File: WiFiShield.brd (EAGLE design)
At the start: 68.6 x 53.3 mm, 38 parts, among them IC1 74HC4050D, IC2 SPX3819M5-L-3-3, IC3 CC3000MOD, IC4 MCP9701A, J1 Test, J10 U.FL-R-SMT-1(10), J11 Mode, J12 Temp, J5 ARDUINO-SHIELD_R3, J6 101-00660-68-6

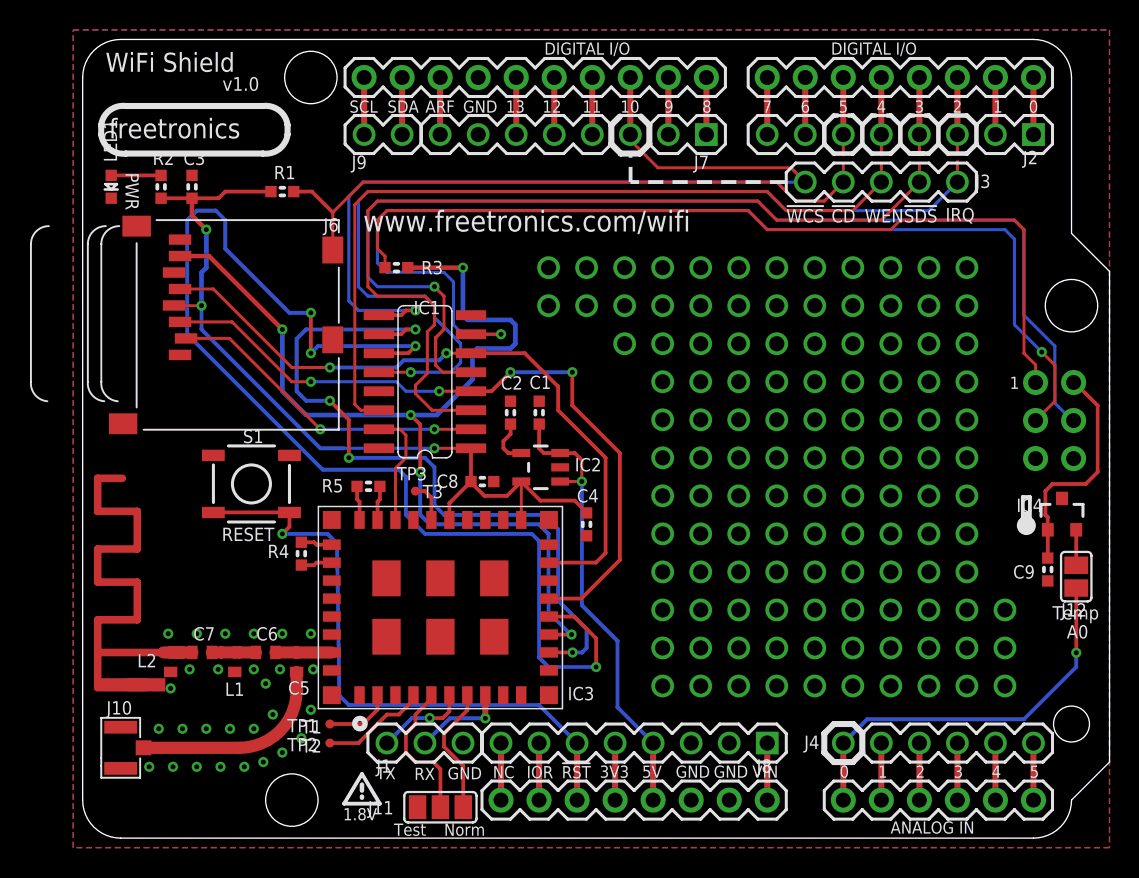
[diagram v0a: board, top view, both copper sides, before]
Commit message: Added tristate buffer on MISO to fix CC3000 SPI bug, some minor tweaks, pull-ups added on nCS lines and CC3000 enable, silkscreen label tweaks.
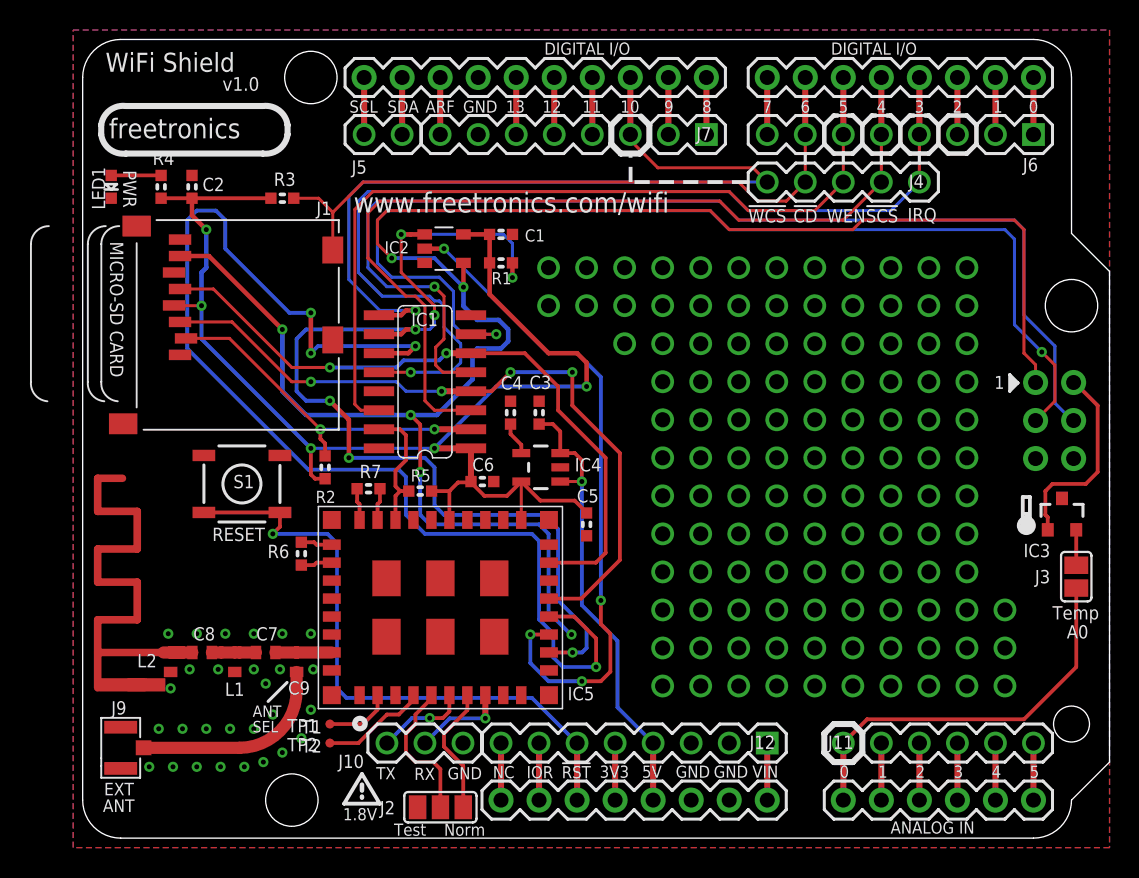
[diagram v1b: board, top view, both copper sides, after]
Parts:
- removed TP3: R3, testpad:TP06R
- added IC5: CC3000MOD, freetronics-luke:CC3000
- added R6, R7: 0R, freetronics-master-v1:0603
- C2: value 10nF -> 100nF
- C4: value 1µF -> 10nF
- C5: value NP -> 1uF; device freetronics-master-v1:C0402 -> freetronics-master-v1:0603
- C6: value 10pF -> 1uF; device freetronics-master-v1:C0402 -> freetronics-master-v1:0603
- C7: value 2.2pF -> 10pF
- C8: value 1µF -> 2.2pF; device freetronics-master-v1:0603 -> freetronics-master-v1:C0402
- C9: value 100nF -> NP; device freetronics-master-v1:0603 -> freetronics-master-v1:C0402
- IC2: value SPX3819M5-L-3-3 -> 74AHC1G125; device SparkFun:SOT23-5 -> 74xx-little-de:SOT23-5
- IC3: value CC3000MOD -> MCP9701A; device freetronics-luke:CC3000 -> freetronics-master-v1:SOT23-3
- IC4: value MCP9701A -> SPX3819M5-L-3-3; device freetronics-master-v1:SOT23-3 -> SparkFun:SOT23-5
- J1: value Test -> 101-00660-68-6; device freetronics-master-v1:1X03 -> RAMPSdisplay:ADAFRUIT_MICROSD
- J10: value U.FL-R-SMT-1(10) -> Test; device freetronics-luke:UFL -> freetronics-master-v1:1X03
- J11: value Mode -> (none); device freetronics-master-v1:SJ_2 -> freetronics-master-v1:1X06
- J12: value Temp -> (none); device freetronics-luke:SJ -> freetronics-master-v1:1X08
- J2: value (none) -> Mode; device freetronics-master-v1:1X08 -> freetronics-master-v1:SJ_2
- J3: value (none) -> Temp; device freetronics-master-v1:1X05 -> freetronics-luke:SJ
- J4: device freetronics-master-v1:1X06 -> freetronics-master-v1:1X05
- J5: value ARDUINO-SHIELD_R3 -> (none); device freetronics-luke:ARDUINO-SHIELD_R3 -> freetronics-master-v1:1X02
- J6: value 101-00660-68-6 -> (none); device RAMPSdisplay:ADAFRUIT_MICROSD -> freetronics-master-v1:1X08
- J8: value (none) -> ARDUINO-SHIELD_R3; device freetronics-master-v1:1X08 -> freetronics-luke:ARDUINO-SHIELD_R3
- J9: value (none) -> U.FL-R-SMT-1(10); device freetronics-master-v1:1X02 -> freetronics-luke:UFL
- R1: value 10kΩ -> 10k
- R2, R3: value 1kΩ -> 10k
- R4: value 0Ω -> 1k
- R5: value 0Ω -> 10k
- moved J2 59.9 mm to (25.8, 2.06), turned to 0 degrees
- moved C9 50.5 mm to (16.2, 11.7), turned to 90 degrees
- moved J6 46.7 mm to (65.4, 47.0), turned to 180 degrees
- moved J9 45.1 mm to (4.45, 6.03)
- moved IC3 42.0 mm to (67.3, 21.6), turned to 0 degrees
- moved J4 37.8 mm to (57.8, 43.8), turned to 180 degrees
- moved J1 35.1 mm to (19.1, 41.3), turned to 270 degrees
- moved IC4 35.0 mm to (32.5, 24.8), turned to 90 degrees
- moved C3 27.7 mm to (32.4, 28.4), turned to 270 degrees
- moved J3 27.5 mm to (68.3, 17.5), turned to 270 degrees
- moved J11 27.2 mm to (52.7, 6.35)
- moved R4 26.2 mm to (7.14, 43.5)
- moved C2 26.1 mm to (9.21, 43.5), turned to 90 degrees
- moved J5 24.8 mm to (23.2, 47.0), turned to 180 degrees
- moved J12 23.4 mm to (47.6, 6.35), turned to 180 degrees
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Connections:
- removed net MISO_3V3: IC3.13, J6.7, R3.1
- removed net MISO_BUFFERED: J5.MISO, R3.2
- removed net N$21: IC1.9, J3.5
- removed net N$3: IC1.15, IC3.26
- removed net N$35: IC1.2, J6.2
- removed net N$41: IC1.10, IC3.12
- removed net RES_3: IC3.24, TP3.TP
- new net !CC3000_CS_3V3: IC1.10, IC2.1, IC5.12, R1.2
- new net !CC3000_CS_5V: IC1.9, J4.5
- new net !SD_CS_3V3: IC1.2, J1.2, R2.2
- new net CC3000_EN_3V3: IC1.15, IC5.26, R5.2
- new net CC3000_MISO: IC2.2, IC5.13
- new net MISO_TRISTATE: IC2.4, J1.7, J8.MISO
- net !CARD_DET: now also J1.CD1, J4.4, R3.1; no longer J3.4, J6.CD1, R1.1
- net !SDCARD_CS_5V: now also J4.2; no longer J3.2
- net +3V3: now also C1.2, C2.1, C5.1, C6.2, IC4.5, IC5.19, IC5.23, J1.4, R1.1, R2.1, R3.2, R4.2, R5.1; no longer C3.1, C4.1, C8.2, IC3.19, IC3.23, J6.4, R1.2, R2.2
- net +5V: now also C3.2, IC4.1, IC4.3, J12.4, J8.+5V; no longer C1.2, IC2.1, IC2.3, J5.+5V, J8.4
- net +5V-2: now also IC3.1, J8.+5V@0; no longer C9.1, IC4.1, J5.+5V@0
- net A0: now also J11.1, J3.2, J8.A0; no longer J12.2, J4.1, J5.A0
- net CC3000_EN_5V: now also J4.3; no longer J3.3
- net CC3000_IRQ_5V: now also J4.1; no longer J3.1
- net GND: now also C2.2, C3.1, C4.1, C5.2, C6.1, IC2.3, IC3.3, IC4.2, IC5.1, IC5.10, IC5.11, IC5.16, IC5.18, IC5.20, IC5.21, IC5.22, IC5.25, IC5.31, IC5.32, IC5.33, IC5.34, IC5.36, IC5.37, IC5.38, IC5.39, IC5.40, IC5.41, IC5.42, IC5.43, IC5.44, IC5.45, IC5.46, IC5.9, J1.6, J1.MT1, J1.MT2, J10.3, J12.2, J12.3, J2.1, J8.GND, J8.GND@0, J8.GND@1, J8.GND@2, J9.GND, J9.GND@1; no longer C2.1, C3.2, C4.2, C8.1, C9.2, IC2.2, IC3.1, IC3.10, IC3.11, IC3.16, IC3.18, IC3.20, IC3.21, IC3.22, IC3.25, IC3.31, IC3.32, IC3.33, IC3.34, IC3.36, IC3.37, IC3.38, IC3.39, IC3.40, IC3.41, IC3.42, IC3.43, IC3.44, IC3.45, IC3.46, IC3.9, IC4.3, J1.3, J10.GND, J10.GND@1, J11.1, J5.GND, J5.GND@0, J5.GND@1, J5.GND@2, J6.6, J6.MT1, J6.MT2, J8.2, J8.3
- net MOSI_3V3: now also IC5.15, J1.3; no longer IC3.15, J6.3
- net MOSI_5V: now also J8.MOSI; no longer J5.MOSI
- net N$1: now also IC5.27, R7.2; no longer IC3.27, R5.2
- net N$103: now also C7.1, C8.2; no longer C6.1, C7.2
- net N$104: now also C8.1; no longer C7.1
- net N$11: now also IC3.2, J3.1; no longer IC4.2, J12.1
- net N$123: now also J6.6, J8.D5; no longer J2.6, J5.D5
- net N$124: now also J6.7, J8.D6; no longer J2.7, J5.D6
- net N$125: now also J6.8, J8.D7; no longer J2.8, J5.D7
- net N$126: now also J5.1, J8.SDA; no longer J5.SDA, J9.1
- net N$127: now also J8.AREF; no longer J5.AREF
- net N$128: now also J8.D13; no longer J5.D13
- net N$129: now also J8.D12; no longer J5.D12
- net N$130: now also J5.2, J8.SCL; no longer J5.SCL, J9.2
- net N$131: now also J8.D8; no longer J5.D8
- net N$132: now also J8.D9; no longer J5.D9
- net N$133: now also J8.D10; no longer J5.D10
- net N$134: now also J8.D11; no longer J5.D11
- net N$15: now also IC5.30, R6.2; no longer IC3.30, R4.2
- net N$16: now also C7.2, C9.2, IC5.35; no longer C5.2, C6.2, IC3.35
- net N$2: now also IC5.28, R7.1; no longer IC3.28, R5.1
- net N$28: now also IC5.4; no longer IC3.4
- net N$29: now also IC5.2; no longer IC3.2
- net N$30: now also C9.1, J9.SIG; no longer C5.1, J10.SIG
- net N$4: now also R4.1; no longer R2.1
- net N$42: now also IC5.14; no longer IC3.14
- net N$43: now also C4.2, IC4.4; no longer C2.2, IC2.4
- net N$48: now also J11.2, J8.A1; no longer J4.2, J5.A1
- net N$49: now also J11.3, J8.A2; no longer J4.3, J5.A2
- net N$5: now also IC5.29, R6.1; no longer IC3.29, R4.1
- net N$50: now also J11.4, J8.A3; no longer J4.4, J5.A3
- net N$72: now also J11.5, J8.A4; no longer J4.5, J5.A4
- net N$73: now also J11.6, J8.A5; no longer J4.6, J5.A5
- net N$74: now also J12.8, J8.RESERVED; no longer J5.RESERVED, J8.8
- net N$75: now also J12.1, J8.VIN; no longer J5.VIN, J8.1
- net N$77: now also J12.5, J8.3V3; no longer J5.3V3, J8.5
- net N$78: now also J12.6, J8.!RESET; no longer J5.!RESET, J8.6
- net N$81: now also J12.7, J8.IOREF; no longer J5.IOREF, J8.7
- net N$82: now also J6.1, J8.D0; no longer J2.1, J5.D0
- net N$87: now also J6.2, J8.D1; no longer J2.2, J5.D1
- net N$88: now also J6.3, J8.D2; no longer J2.3, J5.D2
- net N$89: now also J6.4, J8.D3; no longer J2.4, J5.D3
- net N$90: now also J6.5, J8.D4; no longer J2.5, J5.D4
- net SCK_3V3: now also IC5.17, J1.5; no longer IC3.17, J6.5
- net SCK_5V: now also J8.SCK; no longer J5.SCK
- net WL_EN1: now also IC5.7, J2.3; no longer IC3.7, J11.3
- net WL_EN2: now also IC5.5, J2.2; no longer IC3.5, J11.2
- net WL_UART_RX: now also IC5.8, J10.2; no longer IC3.8, J1.2
- net WL_UART_TX: now also IC5.6, J10.1; no longer IC3.6, J1.1
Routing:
- net MISO_TRISTATE: track 0.00 -> 126.1 mm, vias 0 -> 6
- net !CC3000_CS_3V3: track 0.00 -> 72.3 mm, vias 0 -> 7
- net MISO_3V3: track 69.0 -> 0.00 mm, vias 5 -> 0
- net MISO_BUFFERED: track 58.4 -> 0.00 mm
- net N$21: track 58.1 -> 0.00 mm, vias 1 -> 0
- net !CC3000_CS_5V: track 0.00 -> 52.2 mm, vias 0 -> 1
- net N$41: track 49.9 -> 0.00 mm, vias 4 -> 0
- net CC3000_MISO: track 0.00 -> 44.5 mm, vias 0 -> 4
- net +3V3: track 57.3 -> 89.5 mm, vias 3 -> 5
- net !SD_CS_3V3: track 0.00 -> 23.5 mm, vias 0 -> 2
- net N$35: track 21.5 -> 0.00 mm, vias 2 -> 0
- net CC3000_EN_3V3: track 0.00 -> 8.75 mm
- net N$3: track 7.92 -> 0.00 mm
- net N$124: track 3.81 -> 6.83 mm
- net RES_3: track 2.74 -> 0.00 mm
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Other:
- board text added: "!SCS"
- board text added: "ANT"
- board text added: "EXT"
- board text added: "MICRO-SD CARD"
- board text added: "SEL"
- board text removed: "T3"

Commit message: Swap adafruit microsd slot for (very similar) freetronics library footprint, remove sometimes-problematic CD line
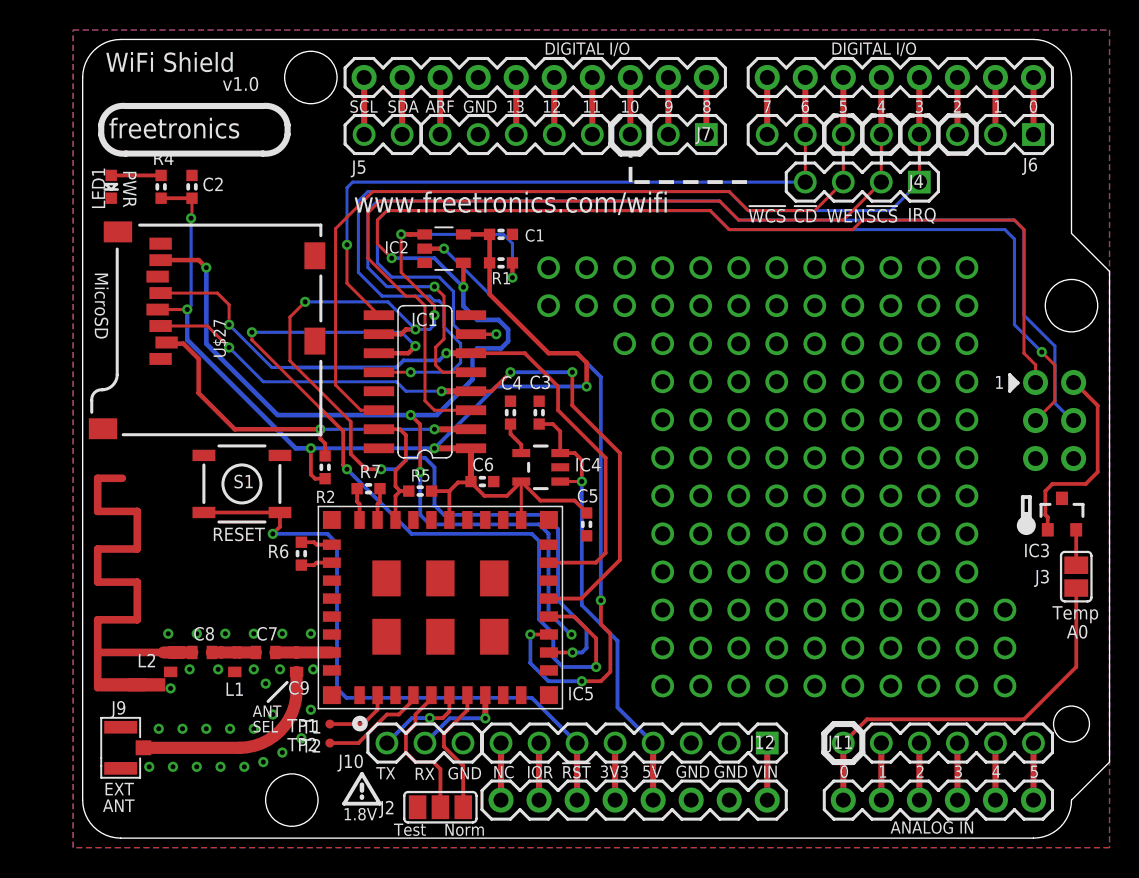
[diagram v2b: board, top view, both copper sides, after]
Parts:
- removed J1: 101-00660-68-6, RAMPSdisplay:ADAFRUIT_MICROSD
- removed R3: 10k, freetronics-master-v1:0603
- added U$27: USD-SOCKETNEW, freetronics-master-v1.1:MICRO-SD-SOCKET-PP
- J4: device freetronics-master-v1:1X05 -> freetronics-master-v1.1:1X04
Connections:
- net N$81 renamed IOREF
- removed net !CARD_DET: J1.CD1, J4.4, R3.1
- net !CC3000_CS_5V: now also J4.4; no longer J4.5
- net !SD_CS_3V3: now also U$27.2; no longer J1.2
- net +3V3: now also U$27.4; no longer J1.4, R3.2
- net GND: now also U$27.6, U$27.GND1, U$27.GND2; no longer J1.6, J1.MT1, J1.MT2
- net MISO_TRISTATE: now also U$27.7; no longer J1.7
- net MOSI_3V3: now also U$27.3; no longer J1.3
- net SCK_3V3: now also U$27.5; no longer J1.5
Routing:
- net !CARD_DET: track 39.0 -> 0.00 mm
- net N$42: track 80.8 -> 57.6 mm
- net !CC3000_CS_5V: track 52.2 -> 40.2 mm
- net !CC3000_CS_3V3: track 72.3 -> 74.9 mm
- net +3V3: track 89.5 -> 87.0 mm
- net !SD_CS_3V3: track 23.5 -> 26.0 mm
- net SCK_3V3: track 45.2 -> 47.2 mm
- net MISO_TRISTATE: track 126.1 -> 127.8 mm
- net MOSI_3V3: track 48.3 -> 49.5 mm
- net CC3000_EN_5V: track 52.2 -> 53.3 mm
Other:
- board text added: "MicroSD"
- board text removed: "MICRO-SD CARD"

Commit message: Swap 4050 buffer for MC74VHCT50A (stocked part, used on FTOLED.)
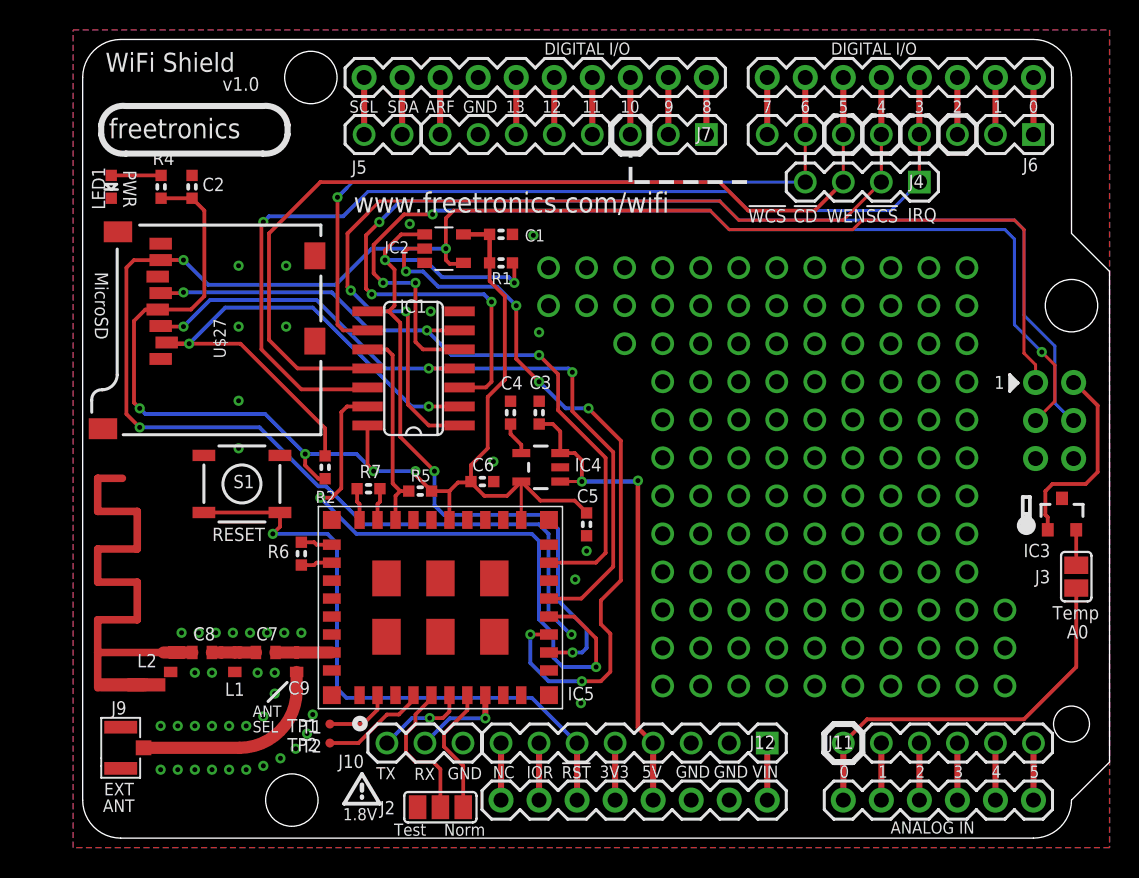
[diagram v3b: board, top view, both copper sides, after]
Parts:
- IC1: device 40xx:SO16 -> freetronics-angus:SO14
- moved IC1 1.17 mm to (24.0, 31.4)
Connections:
- net !CC3000_CS_3V3: now also IC1.8; no longer IC1.10
- net !SDCARD_CS_5V: now also IC1.1; no longer IC1.3
- net +3V3: now also IC1.14; no longer IC1.1
- net CC3000_EN_3V3: now also IC1.10; no longer IC1.15
- net CC3000_EN_5V: now also IC1.11; no longer IC1.14
- net GND: now also IC1.7; no longer IC1.8
- net MOSI_5V: now also IC1.3; no longer IC1.5
- net N$42: now also IC1.13; no longer IC1.11
- net SCK_5V: now also IC1.5; no longer IC1.7
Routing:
- net !CC3000_CS_3V3: track 74.9 -> 54.1 mm, vias 7 -> 4
- net N$42: track 57.6 -> 41.4 mm, vias 4 -> 2
- net !SD_CS_3V3: track 26.0 -> 36.6 mm
- net CC3000_EN_5V: track 53.3 -> 58.8 mm
- net CC3000_EN_3V3: track 8.75 -> 13.8 mm
- net CC3000_MISO: track 44.5 -> 49.4 mm, vias 4 -> 6
- net MOSI_5V: track 76.1 -> 80.1 mm, vias 1 -> 3
- net SCK_5V: track 73.1 -> 70.5 mm, vias 2 -> 4
- net +3V3: track 87.0 -> 84.4 mm, vias 5 -> 4
- net !SDCARD_CS_5V: track 57.0 -> 59.6 mm, vias 0 -> 2
- net CC3000_IRQ_5V: track 63.4 -> 65.8 mm
- net +5V: track 30.8 -> 33.1 mm, vias 1 -> 2
- net !CC3000_CS_5V: track 40.2 -> 42.3 mm
- net MOSI_3V3: track 49.5 -> 51.6 mm, vias 4 -> 3
- net SCK_3V3: track 47.2 -> 48.3 mm, vias 2 -> 3
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
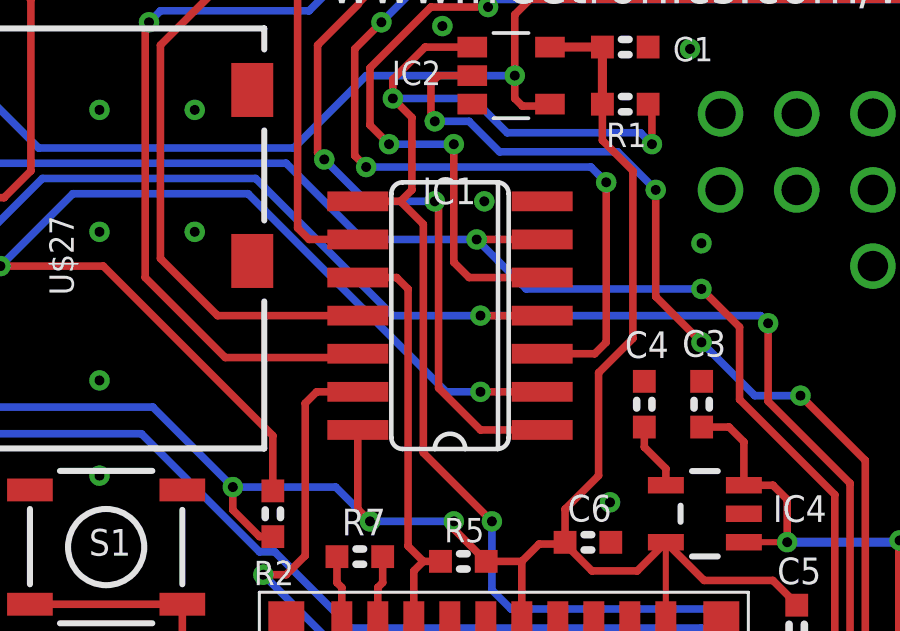
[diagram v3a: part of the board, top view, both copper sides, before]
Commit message: Fixups for MC74VHCT
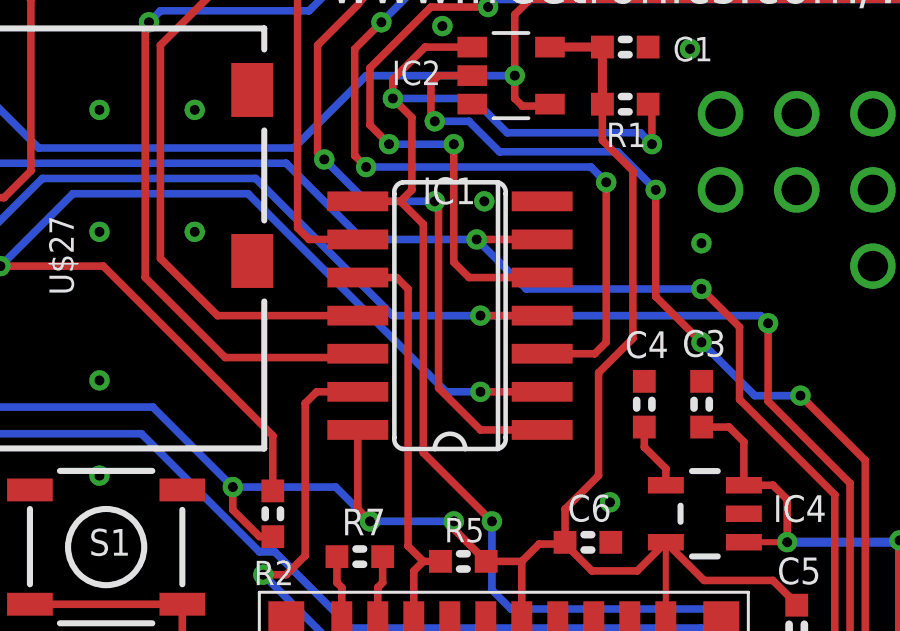
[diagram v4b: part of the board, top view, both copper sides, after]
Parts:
- IC1: value 74HC4050D -> MC74VHCT50A
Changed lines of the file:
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@@
 </element>
 <element name="ANT1" library="adafruit" package="RN-ANT" value="ANTENNA" x="7.3025" y="10.239375" smashed="yes"/>
-<element name="IC1" library="freetronics-angus" package="SO14" value="74HC4050D" x="24.003" y="31.369" smashed="yes" rot="R90">
+<element name="IC1" library="freetronics-angus" package="SO14" value="MC74VHCT50A" x="24.003" y="31.369" smashed="yes" rot="R90">
 <attribute name="PACKAGE" value="16-SOIC" x="24.003" y="31.369" size="1.778" layer="27" rot="R90" display="off"/>
 <attribute name="VALUE" x="20.574" y="36.449" size="0.889" layer="27" ratio="15"/>

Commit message: Remove temp sensor
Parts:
- removed IC3: MCP9701A, freetronics-master-v1:SOT23-3
- removed J3: Temp, freetronics-luke:SJ
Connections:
- removed net +5V-2: IC3.1, J8.+5V@0
- removed net N$11: IC3.2, J3.1
- new net N$3: IC1.10
- net A0: no longer J3.2
- net CC3000_EN_3V3: no longer IC1.10
- net GND: no longer IC3.3
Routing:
- net A0: track 26.7 -> 3.81 mm
- net +5V-2: track 13.4 -> 0.00 mm
- net N$11: track 2.37 -> 0.00 mm, vias 0 -> 1
- net CC3000_EN_3V3: track 13.8 -> 12.5 mm
- net N$78: track 42.3 -> 42.9 mm
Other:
- board text removed: "A0"
- board text removed: "Temp"
